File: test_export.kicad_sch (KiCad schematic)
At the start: 2 parts, among them U1 TestMCU

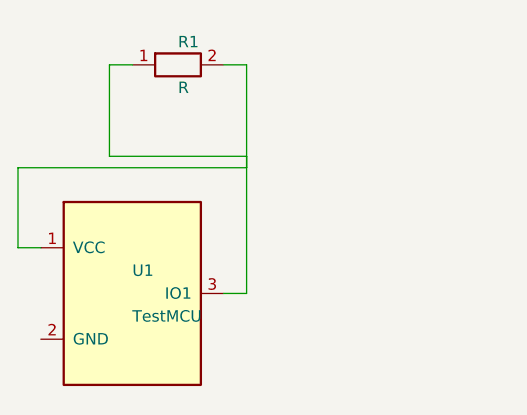
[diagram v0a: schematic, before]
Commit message: Add PCB ratsnest (MST airwires), interaction state machine, single-level undo, and agent validation infrastructure
- pcb_design/ratsnest.py: MST ratsnest generator (Kruskal's, union-find)
- pcb_design/board_model.py: nets normalization (canonical {name, pins}), get_pads_for_net()
- pcb_design/pcb_import.py: pin map building from KiCad AST
- pcb_design/router2.py: handle both 'name' and 'net' net key formats
- server.py: POST /api/ratsnest endpoint
- static/pcb_viewer.js: PCB_MODE state machine (IDLE|PANNING|DRAW_TRACE), ratsnest fetch/render, pad hit-test, single-level undo (Ctrl+Z), Escape cancel
- static/app.js: global keyboard shortcuts for PCB mode, tab switching
- static/index.html: PCB tab UI updates, floatingRouteInput
- tests/test_ratsnest.py: 6 tests for MST logic, trace-collapsed grouping, edge cases
- agent/: new validation modules for connectivity, power nets, structural nets, symbols
- agent/exceptions.py, component_knowledge.py: agent error handling and component knowledge base
- agent/validation.py: validation pipeline for schematic generation
- .gitignore: add .claude/ directory
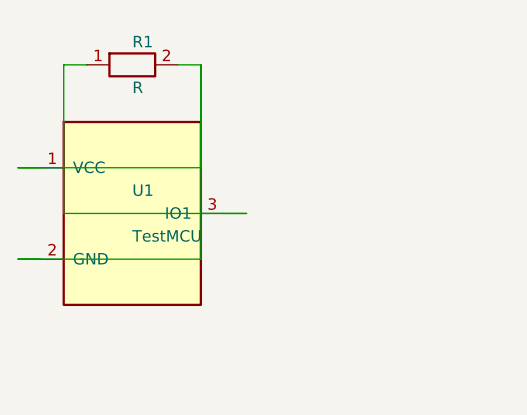
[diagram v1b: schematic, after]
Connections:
- net at R1.2, U1.1 (VCC): now also U1.2 (GND); no longer R1.1, U1.3 (IO1)
- new net: R1.1, U1.3 (IO1)
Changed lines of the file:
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@@
   (title_block
     (title "CircuitBot Generated Design")
-    (date "2026-06-25")
+    (date "2026-07-01")
     (rev "draft")
     (company "")
     (comment 1 "generated by CircuitBot EDA agent")
   )
-  (symbol (lib_id "MCU_Module:TestMCU") (at 63.5 76.2 0) (unit 1)
+  (symbol (lib_id "MCU_Module:TestMCU") (at 63.5 67.31 0) (unit 1)
     (body_style 1)
     (exclude_from_sim no)
     (in_bom yes) (on_board yes) (in_pos_files yes) (dnp no)
-    (property "Reference" "U1" (at 63.5 73.66 0)
+    (property "Reference" "U1" (at 63.5 64.77 0)
       (effects (font (size 1.27 1.27)) (justify left))
     )
-    (property "Value" "TestMCU" (at 63.5 78.74 0)
+    (property "Value" "TestMCU" (at 63.5 69.85 0)
       (effects (font (size 1.27 1.27)) (justify left))
     )
-    (property "Footprint" "" (at 63.5 76.2 0)
+    (property "Footprint" "" (at 63.5 67.31 0)
       (effects (font (size 1.27 1.27)) hide)
     )
-    (property "Datasheet" "" (at 63.5 76.2 0)
+    (property "Datasheet" "" (at 63.5 67.31 0)
       (effects (font (size 1.27 1.27)) hide)
     )
@@
     (instances
       (project "circuitbot"
-        (path "/89608b8e-64a7-433a-a97b-f3e192fc43a3" (reference "U1") (unit 1))
+        (path "/e2d2dfb5-2496-4b5b-b0d1-eb35d962bc46" (reference "U1") (unit 1))
       )
     )
   )
-  (symbol (lib_id "Device:R") (at 68.58 50.8 0) (unit 1)
+  (symbol (lib_id "Device:R") (at 63.5 50.8 0) (unit 1)
     (body_style 1)
     (exclude_from_sim no)
     (in_bom yes) (on_board yes) (in_pos_files yes) (dnp no)
-    (property "Reference" "R1" (at 68.58 48.26 0)
+    (property "Reference" "R1" (at 63.5 48.26 0)
       (effects (font (size 1.27 1.27)) (justify left))
     )
-    (property "Value" "R" (at 68.58 53.34 0)
+    (property "Value" "R" (at 63.5 53.34 0)
       (effects (font (size 1.27 1.27)) (justify left))
     )
-    (property "Footprint" "" (at 68.58 50.8 0)
+    (property "Footprint" "" (at 63.5 50.8 0)
       (effects (font (size 1.27 1.27)) hide)
     )
-    (property "Datasheet" "" (at 68.58 50.8 0)
+    (property "Datasheet" "" (at 63.5 50.8 0)
       (effects (font (size 1.27 1.27)) hide)
     )
@@
     (instances
       (project "circuitbot"
-        (path "/89608b8e-64a7-433a-a97b-f3e192fc43a3" (reference "R1") (unit 1))
+        (path "/e2d2dfb5-2496-4b5b-b0d1-eb35d962bc46" (reference "R1") (unit 1))
       )
     )
   )
-  (wire (pts (xy 73.66 76.2) (xy 76.2 76.2))
+  (wire (pts (xy 53.34 62.23) (xy 50.8 62.23))
     (stroke (width 0) (type default))
   )
-  (wire (pts (xy 76.2 76.2) (xy 76.2 60.96))
+  (wire (pts (xy 50.8 62.23) (xy 71.12 62.23))
     (stroke (width 0) (type default))
   )
-  (wire (pts (xy 76.2 60.96) (xy 60.96 60.96))
+  (wire (pts (xy 71.12 62.23) (xy 71.12 50.8))
     (stroke (width 0) (type default))
   )
-  (wire (pts (xy 60.96 60.96) (xy 60.96 50.8))
+  (wire (pts (xy 71.12 50.8) (xy 68.58 50.8))
     (stroke (width 0) (type default))
   )
-  (wire (pts (xy 60.96 50.8) (xy 63.5 50.8))
+  (wire (pts (xy 73.66 67.31) (xy 76.2 67.31))
     (stroke (width 0) (type default))
   )
-  (wire (pts (xy 53.34 71.12) (xy 50.8 71.12))
+  (wire (pts (xy 76.2 67.31) (xy 55.88 67.31))
     (stroke (width 0) (type default))
   )
-  (wire (pts (xy 50.8 71.12) (xy 50.8 62.23))
+  (wire (pts (xy 55.88 67.31) (xy 55.88 50.8))
     (stroke (width 0) (type default))
   )
-  (wire (pts (xy 50.8 62.23) (xy 76.2 62.23))
+  (wire (pts (xy 55.88 50.8) (xy 58.42 50.8))
     (stroke (width 0) (type default))
   )
-  (wire (pts (xy 76.2 62.23) (xy 76.2 50.8))
+  (wire (pts (xy 53.34 72.39) (xy 50.8 72.39))
     (stroke (width 0) (type default))
   )
-  (wire (pts (xy 76.2 50.8) (xy 73.66 50.8))
+  (wire (pts (xy 50.8 72.39) (xy 71.12 72.39))
     (stroke (width 0) (type default))
   )
-  # WARNING: possible accidental short at (76.2, 76.2) — 2 wire segments meet at non-pin coordinate
-  # WARNING: possible accidental short at (76.2, 60.96) — 2 wire segments meet at non-pin coordinate
-  # WARNING: possible accidental short at (60.96, 60.96) — 2 wire segments meet at non-pin coordinate
-  # WARNING: possible accidental short at (60.96, 50.8) — 2 wire segments meet at non-pin coordinate
-  # WARNING: possible accidental short at (50.8, 71.12) — 2 wire segments meet at non-pin coordinate
-  # WARNING: possible accidental short at (50.8, 62.23) — 2 wire segments meet at non-pin coordinate
-  # WARNING: possible accidental short at (76.2, 62.23) — 2 wire segments meet at non-pin coordinate
-  # WARNING: possible accidental short at (76.2, 50.8) — 2 wire segments meet at non-pin coordinate
-  # ⚠ KiCad export: 8 potential accidental short(s) detected — review wire vertices at the coordinates above
+  (wire (pts (xy 71.12 72.39) (xy 71.12 50.8))
+    (stroke (width 0) (type default))
+  )
   (sheet_instances (path "/" (page "1")))
 )

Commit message: Overhaul: chat-style agent panel, ANSI zig-zag resistors, routing package refactor, PCB layout fixes
- Redesigned agent panel: card-based tool logs replaced with chat-style
  bubbles (conv-agent-msg, conv-user-msg, conv-error-msg, conv-progress)
- Removed menu bar, Property Inspector, agent status dot/pulse animations
- Added ANSI zig-zag resistor rendering with SymbolStyleOverrides registry
- Body rectangle detection uses pin-tip trigonometry (not largest-area)
- Wire stretching during drag is visual-only until mouseup finalizes data
- Server.py returns event-aware responses (wire_paths only for wire events)
- Removed frontend pruning (delegated to routing package as authority)
- Added routing package: astar, candidates, geometry, path_utils
- Added placement engine: annealing, community detection, SA optimizer
- Added scoring metrics: crossings, alignment, wire length, signal flow
- Added synthesis engine: topology classification, graph building
- Added symbol compatibility & validate-repair nodes
- Added knowledge extractor, pin matcher, power domains
- Added benchmark framework (esp32_sensor, opamp, power_regulator, etc.)
- Added PCB viewer tests, schematic renderer tests
- Added tscircuit bridge integration
- Consolidated routing_solution_v3 into main agent package
- Updated .gitignore for generated *.kicad_pcb/*.kicad_sch files
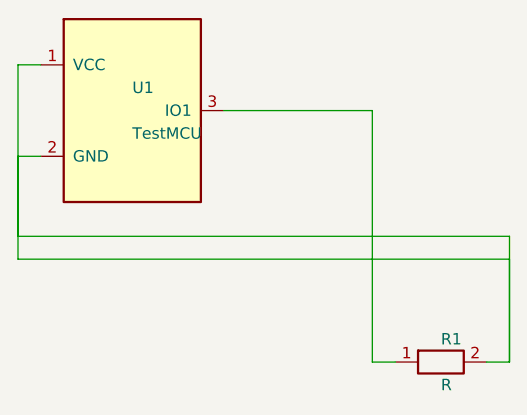
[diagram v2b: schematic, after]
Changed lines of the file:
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@@
   (title_block
     (title "CircuitBot Generated Design")
-    (date "2026-07-01")
+    (date "2026-07-03")
     (rev "draft")
     (company "")
     (comment 1 "generated by CircuitBot EDA agent")
   )
-  (symbol (lib_id "MCU_Module:TestMCU") (at 63.5 67.31 0) (unit 1)
+  (symbol (lib_id "MCU_Module:TestMCU") (at 63.5 55.88 0) (unit 1)
     (body_style 1)
     (exclude_from_sim no)
     (in_bom yes) (on_board yes) (in_pos_files yes) (dnp no)
-    (property "Reference" "U1" (at 63.5 64.77 0)
+    (property "Reference" "U1" (at 63.5 53.34 0)
       (effects (font (size 1.27 1.27)) (justify left))
     )
-    (property "Value" "TestMCU" (at 63.5 69.85 0)
+    (property "Value" "TestMCU" (at 63.5 58.42 0)
       (effects (font (size 1.27 1.27)) (justify left))
     )
-    (property "Footprint" "" (at 63.5 67.31 0)
+    (property "Footprint" "" (at 63.5 55.88 0)
       (effects (font (size 1.27 1.27)) hide)
     )
-    (property "Datasheet" "" (at 63.5 67.31 0)
+    (property "Datasheet" "" (at 63.5 55.88 0)
       (effects (font (size 1.27 1.27)) hide)
     )
@@
     (instances
       (project "circuitbot"
-        (path "/e2d2dfb5-2496-4b5b-b0d1-eb35d962bc46" (reference "U1") (unit 1))
+        (path "/9fb88352-ebb7-4251-854a-3cd059e97e1a" (reference "U1") (unit 1))
       )
     )
   )
-  (symbol (lib_id "Device:R") (at 63.5 50.8 0) (unit 1)
+  (symbol (lib_id "Device:R") (at 97.79 83.82 0) (unit 1)
     (body_style 1)
     (exclude_from_sim no)
     (in_bom yes) (on_board yes) (in_pos_files yes) (dnp no)
-    (property "Reference" "R1" (at 63.5 48.26 0)
+    (property "Reference" "R1" (at 97.79 81.28 0)
       (effects (font (size 1.27 1.27)) (justify left))
     )
-    (property "Value" "R" (at 63.5 53.34 0)
+    (property "Value" "R" (at 97.79 86.36 0)
       (effects (font (size 1.27 1.27)) (justify left))
     )
-    (property "Footprint" "" (at 63.5 50.8 0)
+    (property "Footprint" "" (at 97.79 83.82 0)
       (effects (font (size 1.27 1.27)) hide)
     )
-    (property "Datasheet" "" (at 63.5 50.8 0)
+    (property "Datasheet" "" (at 97.79 83.82 0)
       (effects (font (size 1.27 1.27)) hide)
     )
@@
     (instances
       (project "circuitbot"
-        (path "/e2d2dfb5-2496-4b5b-b0d1-eb35d962bc46" (reference "R1") (unit 1))
+        (path "/9fb88352-ebb7-4251-854a-3cd059e97e1a" (reference "R1") (unit 1))
       )
     )
   )
-  (wire (pts (xy 53.34 62.23) (xy 50.8 62.23))
+  (wire (pts (xy 73.66 55.88) (xy 90.17 55.88))
     (stroke (width 0) (type default))
   )
-  (wire (pts (xy 50.8 62.23) (xy 71.12 62.23))
+  (wire (pts (xy 90.17 55.88) (xy 90.17 83.82))
     (stroke (width 0) (type default))
   )
-  (wire (pts (xy 71.12 62.23) (xy 71.12 50.8))
+  (wire (pts (xy 90.17 83.82) (xy 92.71 83.82))
     (stroke (width 0) (type default))
   )
-  (wire (pts (xy 71.12 50.8) (xy 68.58 50.8))
+  (wire (pts (xy 53.34 60.96) (xy 50.8 60.96))
     (stroke (width 0) (type default))
   )
-  (wire (pts (xy 73.66 67.31) (xy 76.2 67.31))
+  (wire (pts (xy 50.8 60.96) (xy 50.8 72.39))
     (stroke (width 0) (type default))
   )
-  (wire (pts (xy 76.2 67.31) (xy 55.88 67.31))
+  (wire (pts (xy 50.8 72.39) (xy 105.41 72.39))
     (stroke (width 0) (type default))
   )
-  (wire (pts (xy 55.88 67.31) (xy 55.88 50.8))
+  (wire (pts (xy 105.41 72.39) (xy 105.41 83.82))
     (stroke (width 0) (type default))
   )
-  (wire (pts (xy 55.88 50.8) (xy 58.42 50.8))
+  (wire (pts (xy 105.41 83.82) (xy 102.87 83.82))
     (stroke (width 0) (type default))
   )
-  (wire (pts (xy 53.34 72.39) (xy 50.8 72.39))
+  (wire (pts (xy 53.34 50.8) (xy 50.8 50.8))
     (stroke (width 0) (type default))
   )
-  (wire (pts (xy 50.8 72.39) (xy 71.12 72.39))
+  (wire (pts (xy 50.8 50.8) (xy 50.8 69.85))
     (stroke (width 0) (type default))
   )
-  (wire (pts (xy 71.12 72.39) (xy 71.12 50.8))
+  (wire (pts (xy 50.8 69.85) (xy 105.41 69.85))
     (stroke (width 0) (type default))
   )
+  (wire (pts (xy 105.41 69.85) (xy 105.41 83.82))
+    (stroke (width 0) (type default))
+  )
